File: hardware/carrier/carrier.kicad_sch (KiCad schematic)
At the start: 9 parts, among them J1 CAN A -> module J405, J2 CAN B -> module J405, J3 CAN C -> module J405, J4 BRICK A in, J5 BRICK B in, J6 BRICK C in, J7 PWR A -> module J601, J8 PWR B -> module J601, J9 PWR C -> module J601

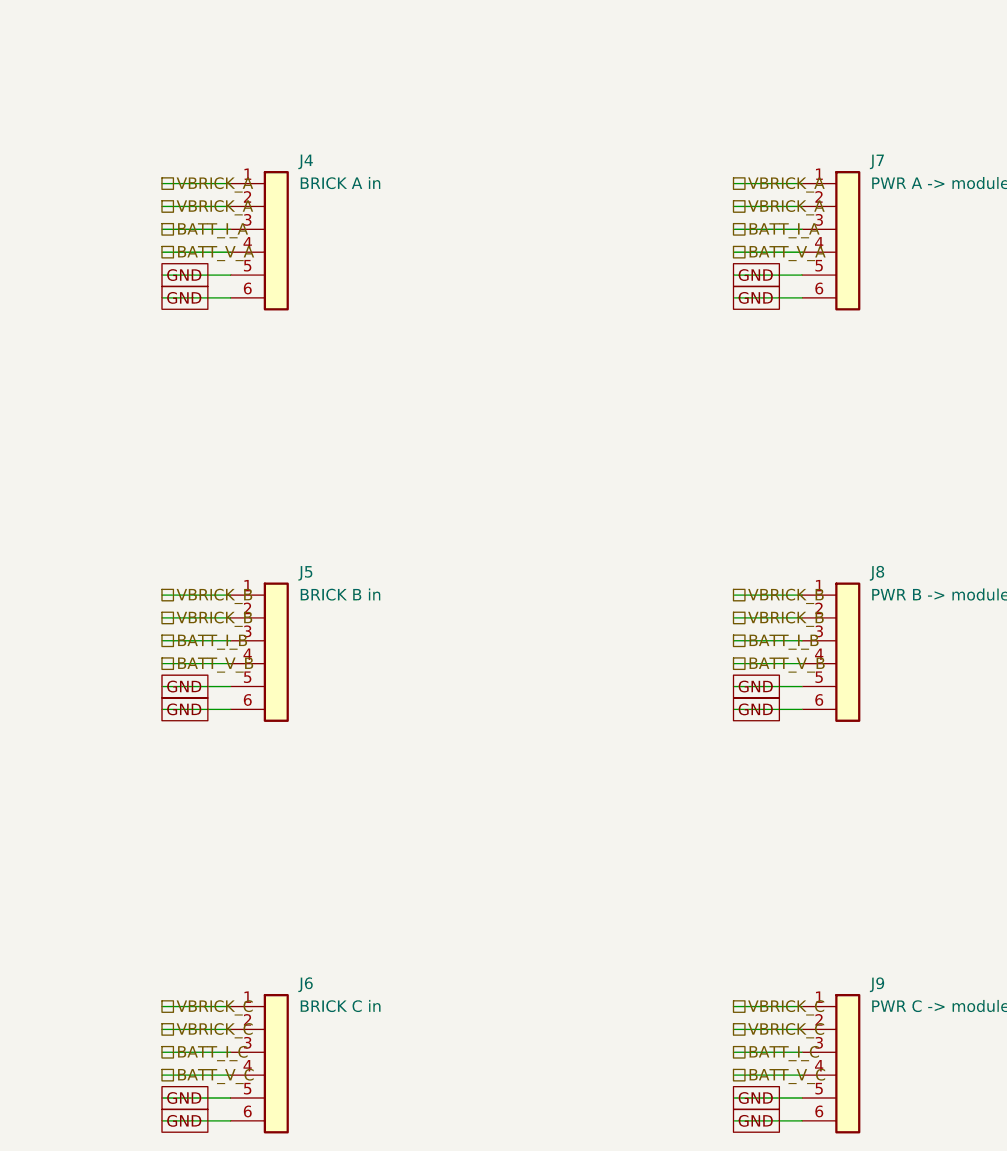
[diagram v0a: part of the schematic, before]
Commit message: Take the carrier from schematic to a DRC-clean board; fix a dangling-net defect
Exporting the carrier as a standalone board netlist exposed a real design
defect: 28 of its nets terminated on a single pin. As a child sheet of
jfox-tmr that reads fine - the net continues into the FMU sheet - but a
pass-through carrier is a path, and half a path is not one. Each board had a
single power connector with nowhere for the power to go.

Redesigned so every signal enters on one connector and leaves on another:
brick power in (J4-J6) -> module J601 out (J7-J9), CAN to the modules
(J1-J3) daisy-chained. Nine connectors, twelve nets, zero single-pin nets.

Two things are deliberately no longer on this board. The servo/PWM breakout
is gone because how three boards' motor commands arbitrate into one output
is still unresolved - TmrVoter is not wired into motor_task - and copper is
the wrong place to record a guess; each module's J901 cables straight to its
ESCs meanwhile. The safety switch is gone because J702's SAFETY lands on
U801.PB5, the IO co-processor this firmware never runs, and neither J405 nor
J601 carries a pin to route it through, so it would have been decorative.

The carrier is now its own KiCad project. It has to be: the three FMU
modules are separately manufactured hardware, and a shared project would
make a board netlist try to place 421 module components on the carrier.

Board work:

- All nine connectors carry real footprints - Hirose DF13 vertical parts
  matching what the modules actually use.
- tools/gen_carrier_pcb.py writes an 80x60 mm two-layer outline with four M3
  holes on a 30.000 x 30.000 mm pattern. That pattern is read from the
  module's own PX4FMUv2.4.5.brd via `kicad-cli pcb import` - board import
  exists on the CLI even though schematic import does not - so a stacked
  module lines up rather than nearly lining up.
- Verified: DRC 0 violations, 0 unconnected. Gerbers, drill and job file all
  export; the drill file contains exactly four 3.2 mm N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
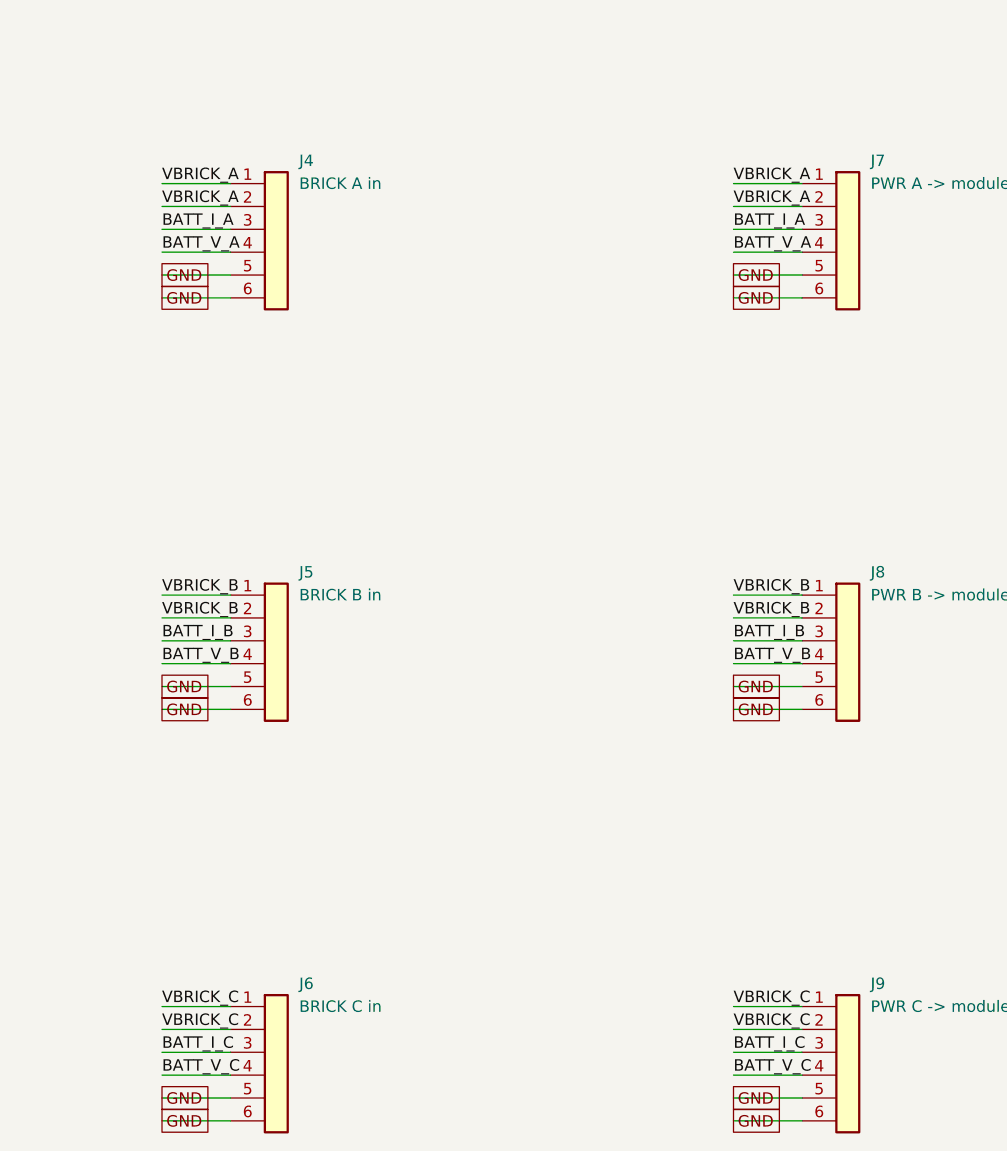
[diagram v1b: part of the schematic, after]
